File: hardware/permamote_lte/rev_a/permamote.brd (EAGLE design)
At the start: 27 x 60 mm, 116 parts, among them IC1 NRF9160, J1 TC2030-JLINK-NL, J2 U.FL-R-SMT, J3 NANO_SIM, J4 U.FL-R-SMT, J5 DM3AT-SF-PEJM5, Q1 PMDXB950UPEL, Q10 PMDXB950UPEL, Q2 PMDXB950UPEL, Q3 PMDXB950UPEL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

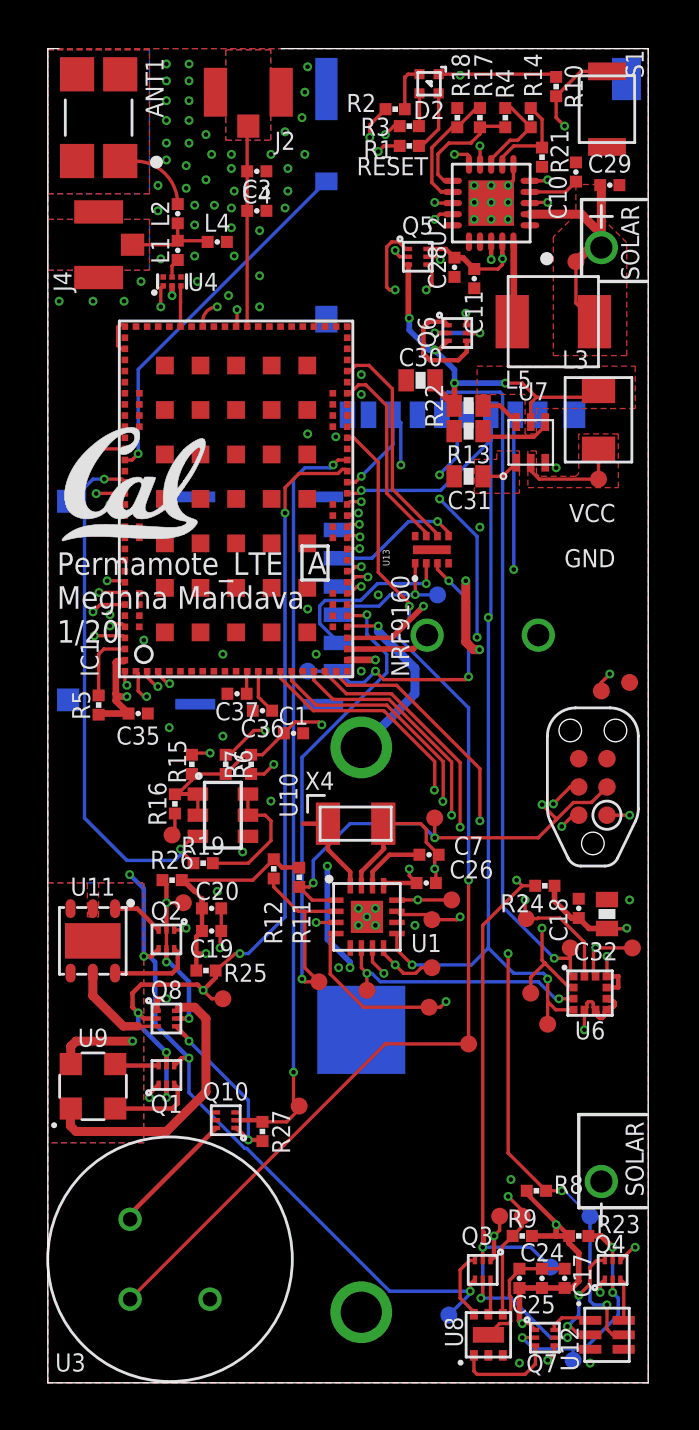
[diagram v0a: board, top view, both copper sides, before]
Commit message: more board fixes
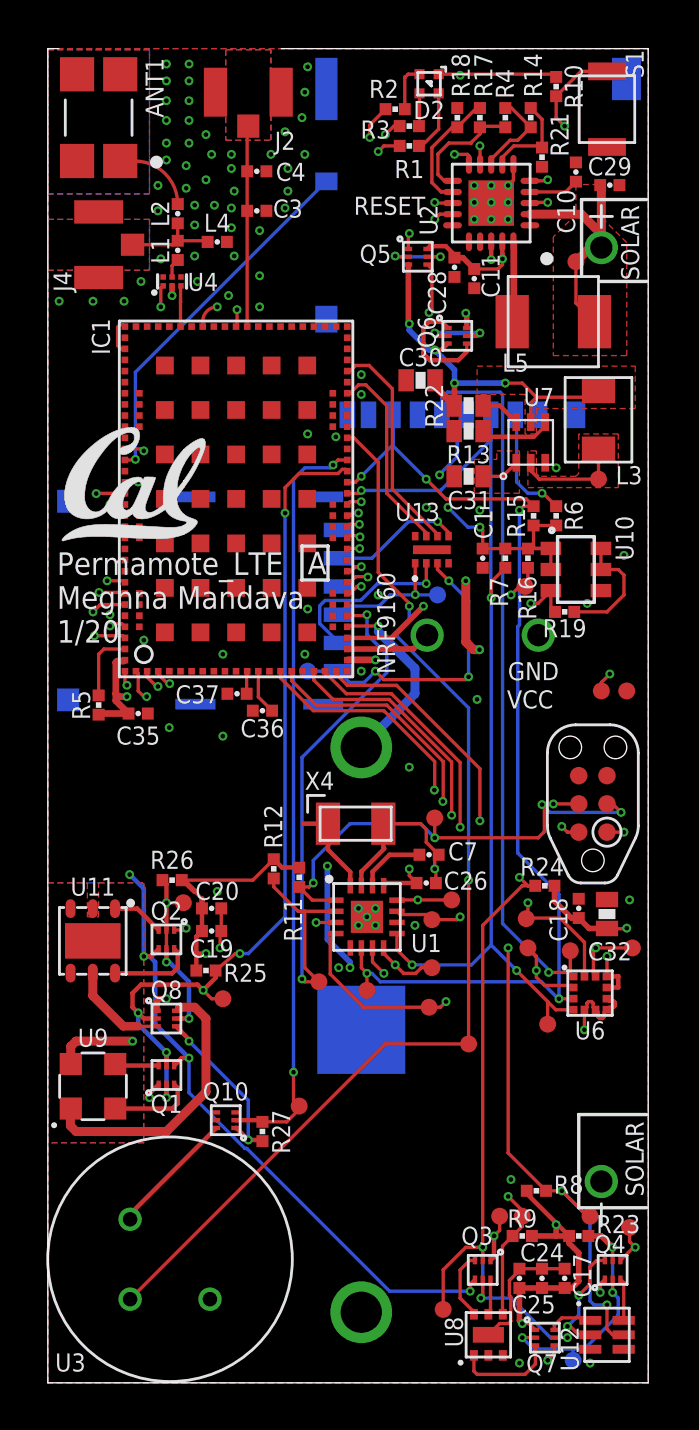
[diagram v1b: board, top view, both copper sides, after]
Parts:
- moved R19 19.8 mm to (23.2, 34.7)
- moved TP32 19.4 mm to (21.5, 35.8)
- moved R16 19.3 mm to (21.6, 37.1)
- moved U10 19.3 mm to (23.7, 36.6)
- moved R15 19.0 mm to (21.8, 39.0)
- moved R6 18.6 mm to (22.9, 39.0)
- moved R7 14.7 mm to (20.6, 37.1)
- moved C1 11.6 mm to (19.6, 37.1), turned to 270 degrees
- moved TP1 9.03 mm to (26.2, 6.99), flipped to the top
- moved TP10 5.19 mm to (17.8, 3.30), flipped to the top
- moved TP7 2.04 mm to (21.6, 19.6)
- moved J1 0.76 mm to (24.5, 26.0)
- moved TP27 0.40 mm to (26.0, 31.1)
- moved Q6 0.13 mm to (18.4, 47.1)
- moved TP3 0.13 mm to (23.5, 19.4)
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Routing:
- net !SD_DETECT: track 17.7 -> 40.2 mm, vias 1 -> 2
- net N$13: track 30.8 -> 14.5 mm, vias 4 -> 3
- net !SD_CS: track 45.9 -> 30.3 mm
- net MOSI: track 59.2 -> 45.6 mm, vias 5 -> 4
- net VCC: track 62.4 -> 66.4 mm, vias 21 -> 23
- net !CLR_INT: track 58.2 -> 59.9 mm
- net MISO: track 51.0 -> 49.5 mm
- net N$45: track 6.17 -> 7.46 mm
- net !RST: track 36.1 -> 37.2 mm, vias 4 -> 5
- net SD_ENABLE: track 24.2 -> 25.0 mm
- net VBAT_OK: track 17.2 -> 17.7 mm

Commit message: mooooooregit add -ugit add -u
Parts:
- moved X4 0.90 mm to (14.7, 25.3)
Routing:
- net GND: track 42.6 -> 40.8 mm, vias 90 -> 91
- net !RTC_EXTR: track 45.6 -> 46.9 mm
- net VCC: track 66.4 -> 67.6 mm
- net !RST: track 37.2 -> 36.7 mm

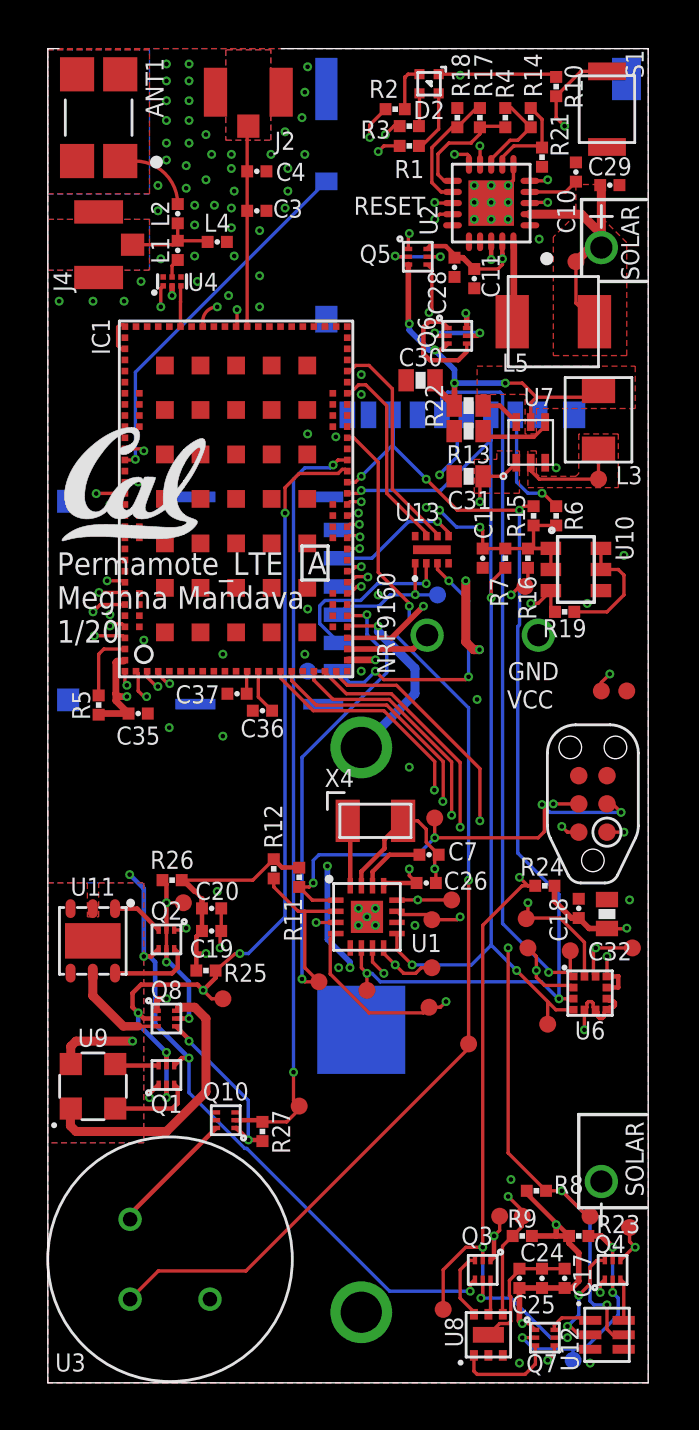
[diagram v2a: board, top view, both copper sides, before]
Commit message: more board fixes
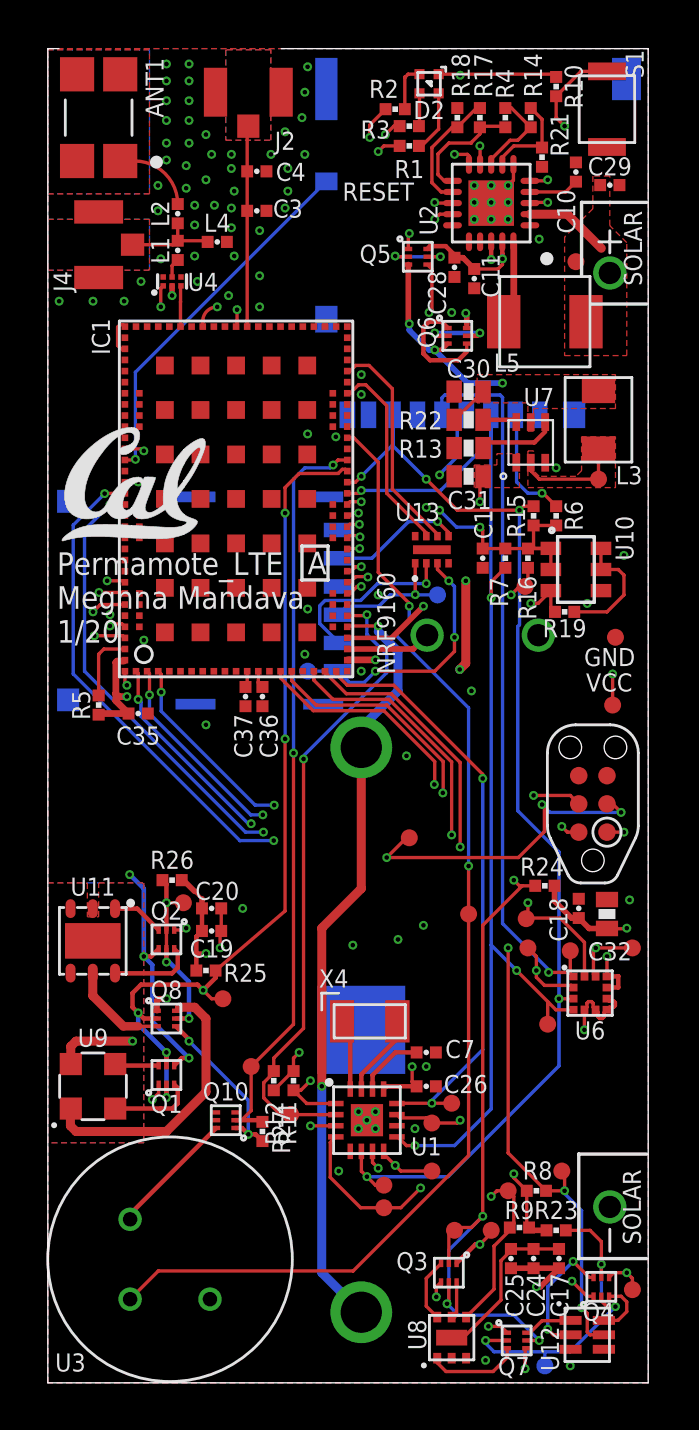
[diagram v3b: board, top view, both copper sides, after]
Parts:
- moved R12 9.53 mm to (10.2, 13.6), turned to 270 degrees
- moved TP14 9.24 mm to (15.1, 7.87)
- moved R11 9.15 mm to (11.0, 13.6)
- moved TP13 9.14 mm to (17.3, 11.7)
- moved TP15 9.14 mm to (17.3, 9.53)
- moved C26 9.14 mm to (17.0, 13.3)
- moved TP6 9.14 mm to (18.2, 12.6)
- moved U1 9.14 mm to (14.4, 11.8)
- moved X4 9.02 mm to (14.5, 16.3)
- moved C7 8.89 mm to (17.0, 14.9)
- moved TP4 8.80 mm to (15.1, 8.89)
- moved TP16 6.10 mm to (10.9, 12.1)
- moved TP22 5.84 mm to (18.9, 21.1)
- moved TP10 3.59 mm to (18.3, 6.86)
- moved TP11 2.80 mm to (9.14, 14.2)
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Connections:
- new net N$40: U1.15, X4.2
- new net N$43: U1.16, X4.1
- net GND: no longer U1.15, U1.16, X4.1, X4.2
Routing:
- net VCC: track 67.6 -> 54.5 mm, vias 23 -> 22
- net SCK: track 66.3 -> 78.5 mm
- net !RST: track 36.7 -> 46.2 mm
- net !RTC_IRQ3: track 21.7 -> 30.9 mm
- net !RTC_IRQ1: track 17.8 -> 26.9 mm
- net GND: track 40.8 -> 32.1 mm, vias 91 -> 94
- net !RTC_EXTR: track 46.9 -> 55.6 mm, vias 2 -> 3
- net VSOL: track 35.8 -> 27.3 mm
- net !RTC_IRQ2: track 27.1 -> 35.2 mm
- net RTC_CS: track 19.1 -> 26.8 mm
- net MOSI: track 45.6 -> 52.4 mm
- net VSW: track 17.7 -> 11.2 mm, vias 4 -> 3
- net MISO: track 49.1 -> 53.9 mm
- net !CLR_INT: track 59.9 -> 55.4 mm, vias 4 -> 5
- net !LT_INT: track 42.1 -> 46.2 mm
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
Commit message: more board fixes
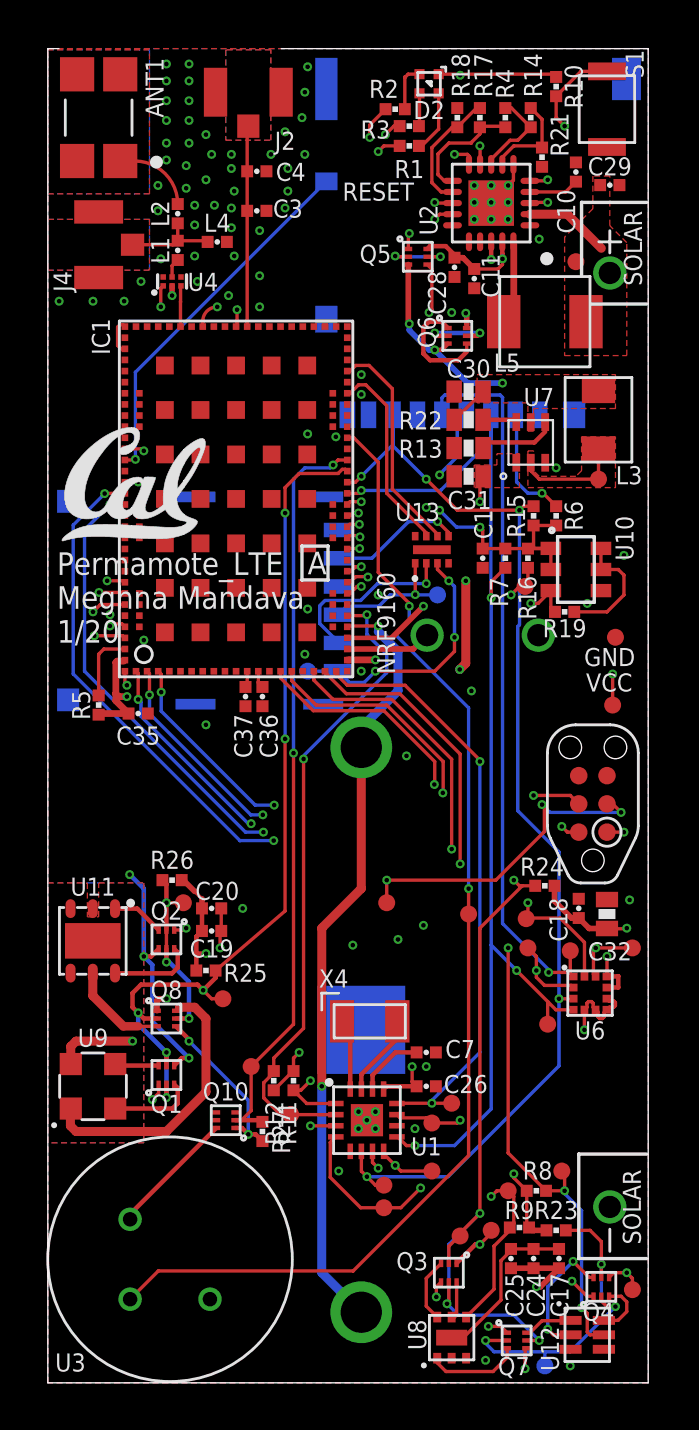
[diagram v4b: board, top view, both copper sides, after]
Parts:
- moved TP17 3.09 mm to (15.2, 21.6)
- moved TP10 0.36 mm to (18.5, 6.60)
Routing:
- net !CLR_INT: track 55.4 -> 56.9 mm
- net !RST: track 46.2 -> 45.2 mm
- net !LT_EN: track 63.1 -> 62.4 mm

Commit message: got rid of erc errors
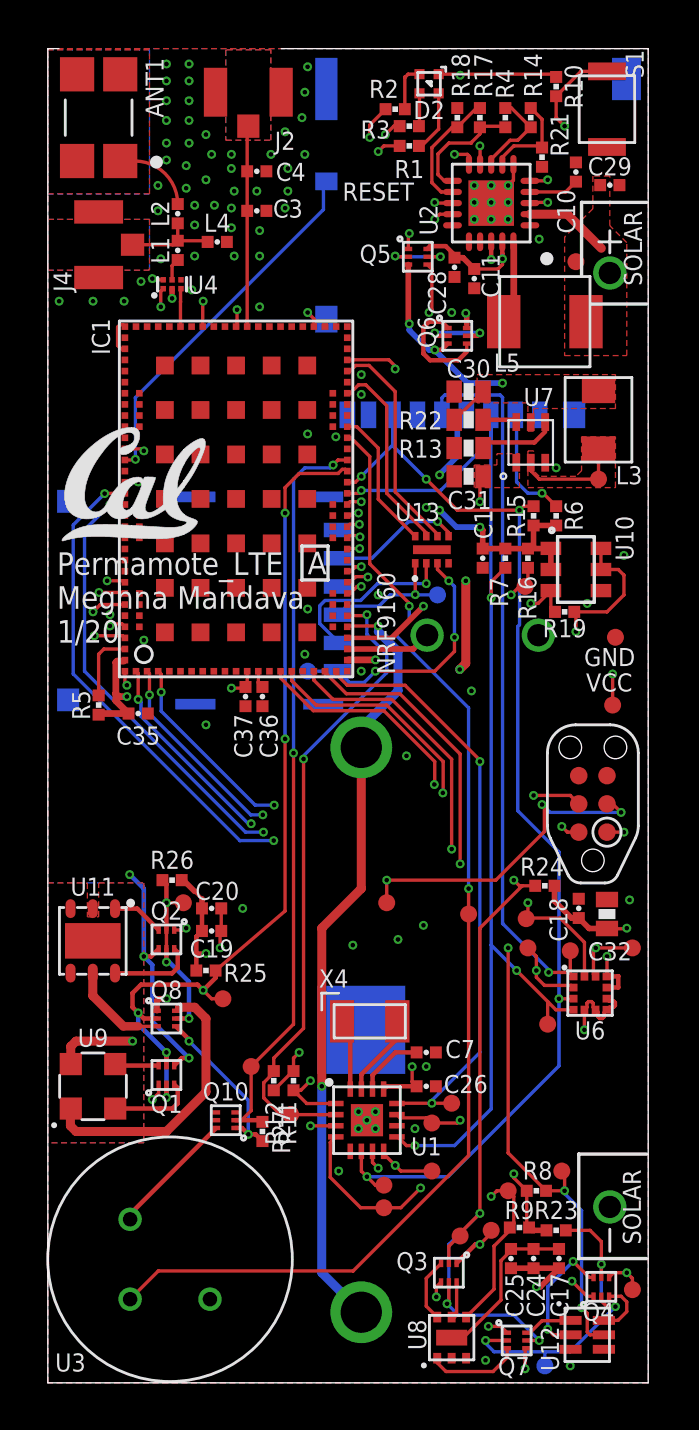
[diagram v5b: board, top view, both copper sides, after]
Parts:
- C3, C4: value (none) -> DNP
- moved U4 0.13 mm to (5.59, 49.4)
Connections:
- removed net +3V3: R19.2, U10.5, U10.6
- removed net N$3: IC1.SIM_DET
- removed net N$33: IC1.SIM_1V8
- removed net N$42: IC1.SIM_RST
- removed net N$6: U4.6
- removed net N$7: C37.1, IC1.VDD_GPIO
- net GPS_EN: now also U4.6
- net SIM_1V8: now also IC1.SIM_1V8
- net SIM_RST: now also IC1.SIM_RST
- net VCC: now also C37.1, IC1.VDD_GPIO, R19.2, U10.5, U10.6
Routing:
- net SIM_1V8: track 6.02 -> 16.4 mm, vias 1 -> 2
- net GPS_EN: track 0.00 -> 8.88 mm, vias 0 -> 2
- net VCC: track 54.5 -> 62.4 mm, vias 22 -> 24
- net SIM_RST: track 0.00 -> 6.44 mm
- net +3V3: track 5.53 -> 0.00 mm
- net N$7: track 0.91 -> 0.00 mm
